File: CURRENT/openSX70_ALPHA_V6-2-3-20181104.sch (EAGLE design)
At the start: 39 parts, among them J1 687106183722, Q1 5.8A/30V/35mΩ, Q2 5.8A/30V/35mΩ, U1 ATMEGA328P_TQFP, Y1 CSTCE8M00G52Z-R0

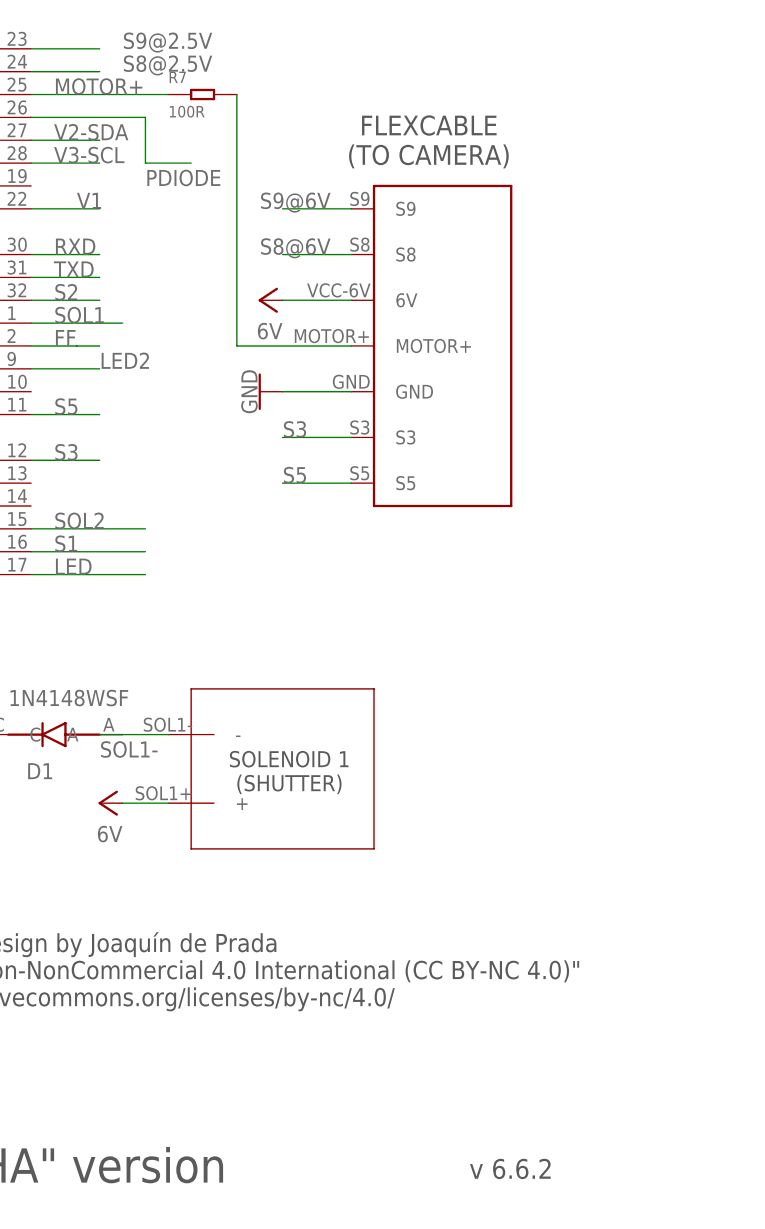
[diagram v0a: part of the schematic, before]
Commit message: changed connector S-pad on 6.2.3
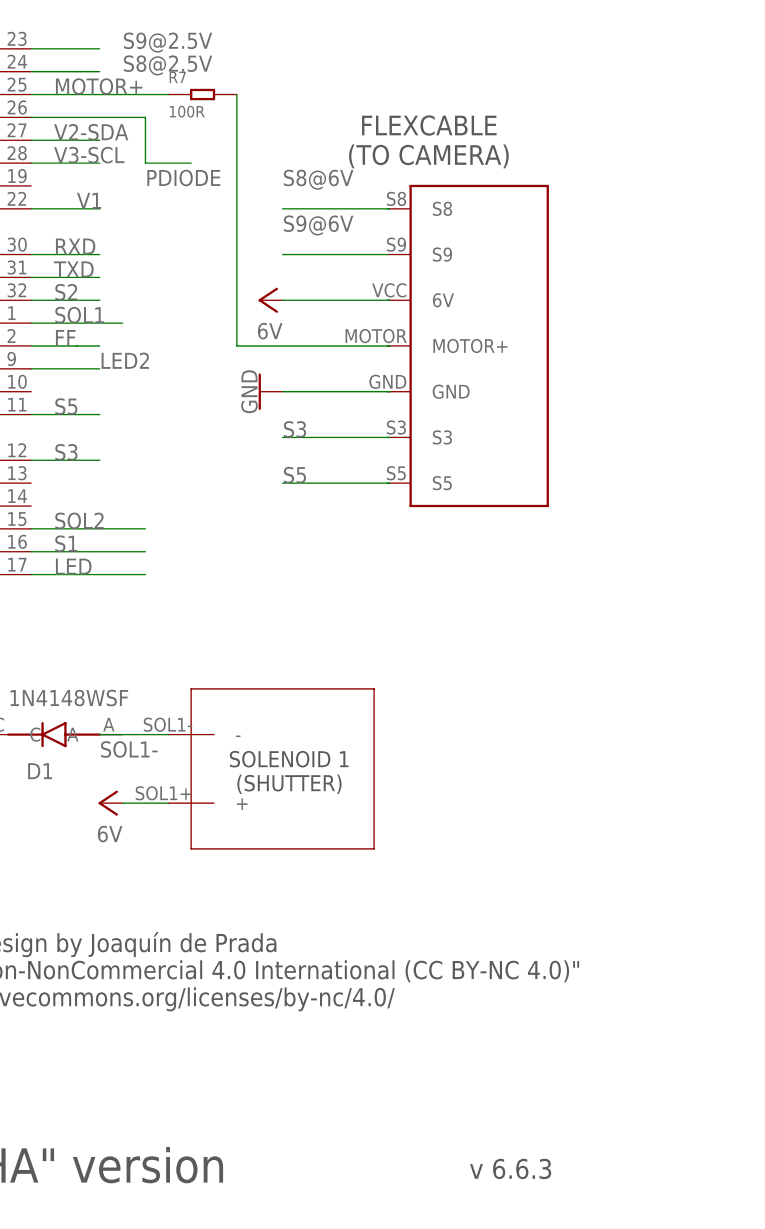
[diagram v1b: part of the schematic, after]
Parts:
- U$1: device openSX70:SX70-7-PAD -> _openSX70:SX70-7-PAD
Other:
- note added: "v 6.6.3"
- note removed: "v 6.6.2"
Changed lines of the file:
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@@
 </classes>
 <parts>
-<part name="U$1" library="openSX70" deviceset="SX70-7-PAD" device=""/>
 <part name="U$2" library="openSX70" deviceset="SX70-FFA-PAD" device="" value="FFA"/>
 <part name="S2+" library="openSX70" deviceset="SX70-S-PAD-NEW" device=""/>
@@
 <part name="R16" library="Seeed-Resistor" library_urn="urn:adsk.eagle:library:474" deviceset="SMD-RES-1K-5%-1/10W(0603)" device="" package3d_urn="urn:adsk.eagle:package:32791/1" value="1K 1/10W"/>
 <part name="GND13" library="supply1" library_urn="urn:adsk.eagle:library:371" deviceset="GND" device=""/>
+<part name="U$1" library="_openSX70" deviceset="SX70-7-PAD" device=""/>
 </parts>
 <sheets>
@@
 or
 FLASH</text>
-<text x="246.38" y="2.54" size="2.1844" layer="97" align="center">v 6.6.2</text>
+<text x="246.38" y="2.54" size="2.1844" layer="97" align="center">v 6.6.3</text>
 <text x="203.454" y="24.638" size="2.0066" layer="97" align="center">Design by Joaquín de Prada
 Creative Commons "Attribution-NonCommercial 4.0 International (CC BY-NC 4.0)"
@@
 </plain>
 <instances>
-<instance part="U$1" gate="G$1" x="238.76" y="93.98" rot="MR0"/>
 <instance part="U$2" gate="G$1" x="20.32" y="134.62"/>
 <instance part="S2+" gate="G$1" x="40.64" y="132.08" rot="R270">
@@
 <attribute name="VALUE" x="27.94" y="7.62" size="1.778" layer="96" rot="R90"/>
 </instance>
+<instance part="U$1" gate="G$1" x="242.824" y="93.98" rot="MR0"/>
 </instances>
 <busses>
@@
 </segment>
 <segment>
+<wire x1="232.664" y1="83.82" x2="220.98" y2="83.82" width="0.1524" layer="91"/>
+<label x="220.98" y="83.82" size="1.778" layer="95"/>
 <pinref part="U$1" gate="G$1" pin="S3"/>
-<wire x1="228.6" y1="83.82" x2="220.98" y2="83.82" width="0.1524" layer="91"/>
-<label x="220.98" y="83.82" size="1.778" layer="95"/>
+<wire x1="232.664" y1="83.82" x2="232.918" y2="83.82" width="0.1524" layer="91"/>
 </segment>
 </net>
@@
 </segment>
 <segment>
+<label x="220.98" y="78.74" size="1.778" layer="95"/>
 <pinref part="U$1" gate="G$1" pin="S5"/>
-<wire x1="228.6" y1="78.74" x2="220.98" y2="78.74" width="0.1524" layer="91"/>
-<label x="220.98" y="78.74" size="1.778" layer="95"/>
+<wire x1="232.664" y1="78.74" x2="220.98" y2="78.74" width="0.1524" layer="91"/>
+<wire x1="232.664" y1="78.74" x2="232.918" y2="78.74" width="0.1524" layer="91"/>
 </segment>
 </net>
@@
 <segment>
 <pinref part="GND2" gate="1" pin="GND"/>
+<wire x1="220.98" y1="88.9" x2="232.664" y2="88.9" width="0.1524" layer="91"/>
 <pinref part="U$1" gate="G$1" pin="GND"/>
-<wire x1="220.98" y1="88.9" x2="228.6" y2="88.9" width="0.1524" layer="91"/>
+<wire x1="232.664" y1="88.9" x2="232.918" y2="88.9" width="0.1524" layer="91"/>
 </segment>
 <segment>
@@
 <segment>
 <pinref part="P+1" gate="VCC" pin="6V"/>
+<wire x1="220.98" y1="99.06" x2="232.664" y2="99.06" width="0.1524" layer="91"/>
 <pinref part="U$1" gate="G$1" pin="6V"/>
-<wire x1="220.98" y1="99.06" x2="228.6" y2="99.06" width="0.1524" layer="91"/>
+<wire x1="232.664" y1="99.06" x2="232.918" y2="99.06" width="0.1524" layer="91"/>
 </segment>
 <segment>
@@
 <net name="MOTOR-HEADER" class="0">
 <segment>
-<pinref part="U$1" gate="G$1" pin="MOTOR+"/>
-<wire x1="228.6" y1="93.98" x2="215.9" y2="93.98" width="0.1524" layer="91"/>
+<wire x1="232.664" y1="93.98" x2="215.9" y2="93.98" width="0.1524" layer="91"/>
 <pinref part="R7" gate="G$1" pin="2"/>
 <wire x1="215.9" y1="121.92" x2="215.9" y2="93.98" width="0.1524" layer="91"/>
+<pinref part="U$1" gate="G$1" pin="MOTOR+"/>
+<wire x1="232.664" y1="93.98" x2="232.918" y2="93.98" width="0.1524" layer="91"/>
 </segment>
 </net>
@@
 </segment>
 <segment>
+<label x="220.98" y="111.76" size="1.778" layer="95"/>
 <pinref part="U$1" gate="G$1" pin="S8"/>
-<wire x1="228.6" y1="104.14" x2="220.98" y2="104.14" width="0.1524" layer="91"/>
-<label x="218.44" y="104.14" size="1.778" layer="95"/>
+<wire x1="232.664" y1="109.22" x2="220.98" y2="109.22" width="0.1524" layer="91"/>
+<wire x1="232.664" y1="109.22" x2="232.918" y2="109.22" width="0.1524" layer="91"/>
 </segment>
 </net>
@@
 </segment>
 <segment>
+<wire x1="232.664" y1="104.14" x2="220.98" y2="104.14" width="0.1524" layer="91"/>
+<label x="220.98" y="106.68" size="1.778" layer="95"/>
 <pinref part="U$1" gate="G$1" pin="S9"/>
-<wire x1="228.6" y1="109.22" x2="220.98" y2="109.22" width="0.1524" layer="91"/>
-<label x="218.44" y="109.22" size="1.778" layer="95"/>
-</segment>
-</net>
+</segment>
+</net>
